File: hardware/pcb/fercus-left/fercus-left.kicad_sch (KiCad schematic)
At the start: 275 parts, among them J1 USB_C_Receptacle_USB2.0, J2 USB_C_Receptacle_USB2.0, J3 Conn_01x06_MountingPin, J5 Conn_01x03, Q1 BSS138, Q10 BSS138, Q2 BSS138, Q3 BSS138, Q4 BSS138, Q5 BSS138, Q6 BSS138, Q7 BSS138, Q8 BSS138, Q9 BSS138, SW1 SW_Push, SW2 SW_Push, SW3 SW_Push, SW4 SW_Push, SW6 SW_Push, SW7 SW_SPDT, SW8 SW_Push, U1 XC6206P332MR, U2 CH32V208CBU6, U3 ETA9084E10, Y1 32MHz, Y2 32.768kHz

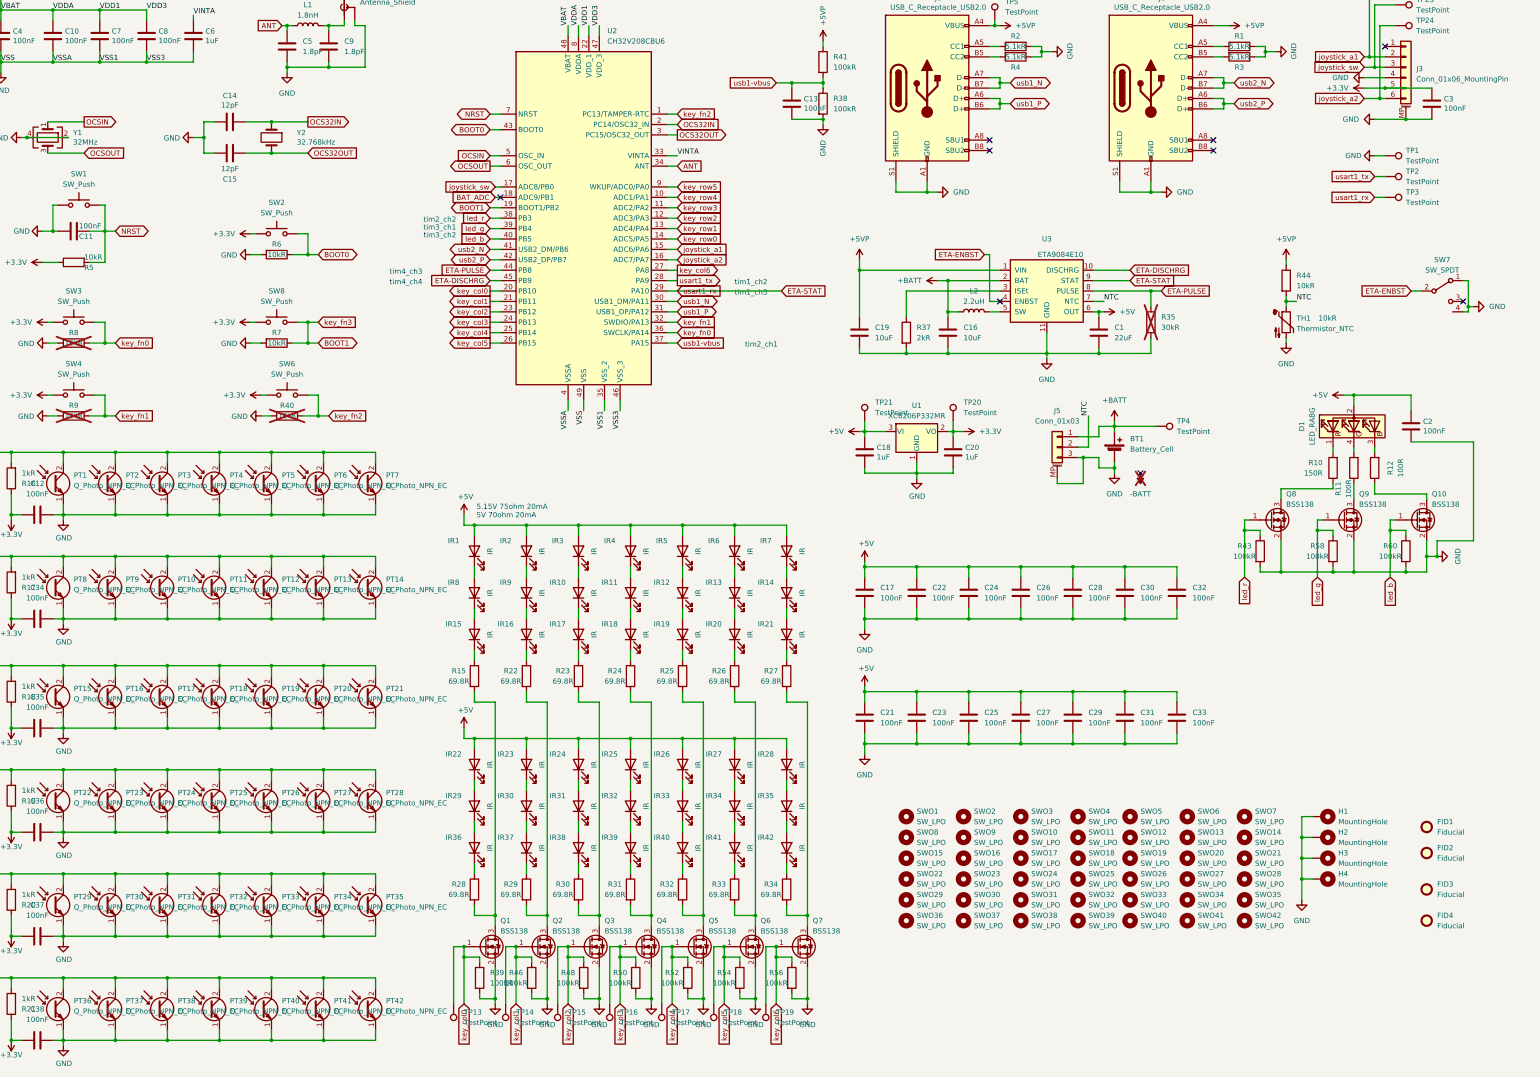
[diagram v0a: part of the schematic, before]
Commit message: merge
    fw:
    - fix usb product string, vid
    - add rf_phy_hop
    - add RF_BondingErase()
    - change default layout key fn to pause
    - fix power manager poweroff when usb disconnect
    - add usb compatibility interface

    hw:
    - change eta9084 iset resistor footprint to 0402
    - change fpc connector part
    - fix ir resistor value
    - change pcb thinkness to 1.6mm
    - fix footprint of pt and ir
    - fix rf ant trace
    - fix usb trace
    - add fercus-dongle-usb-c

    doc:
    - fix layout
    - add manual
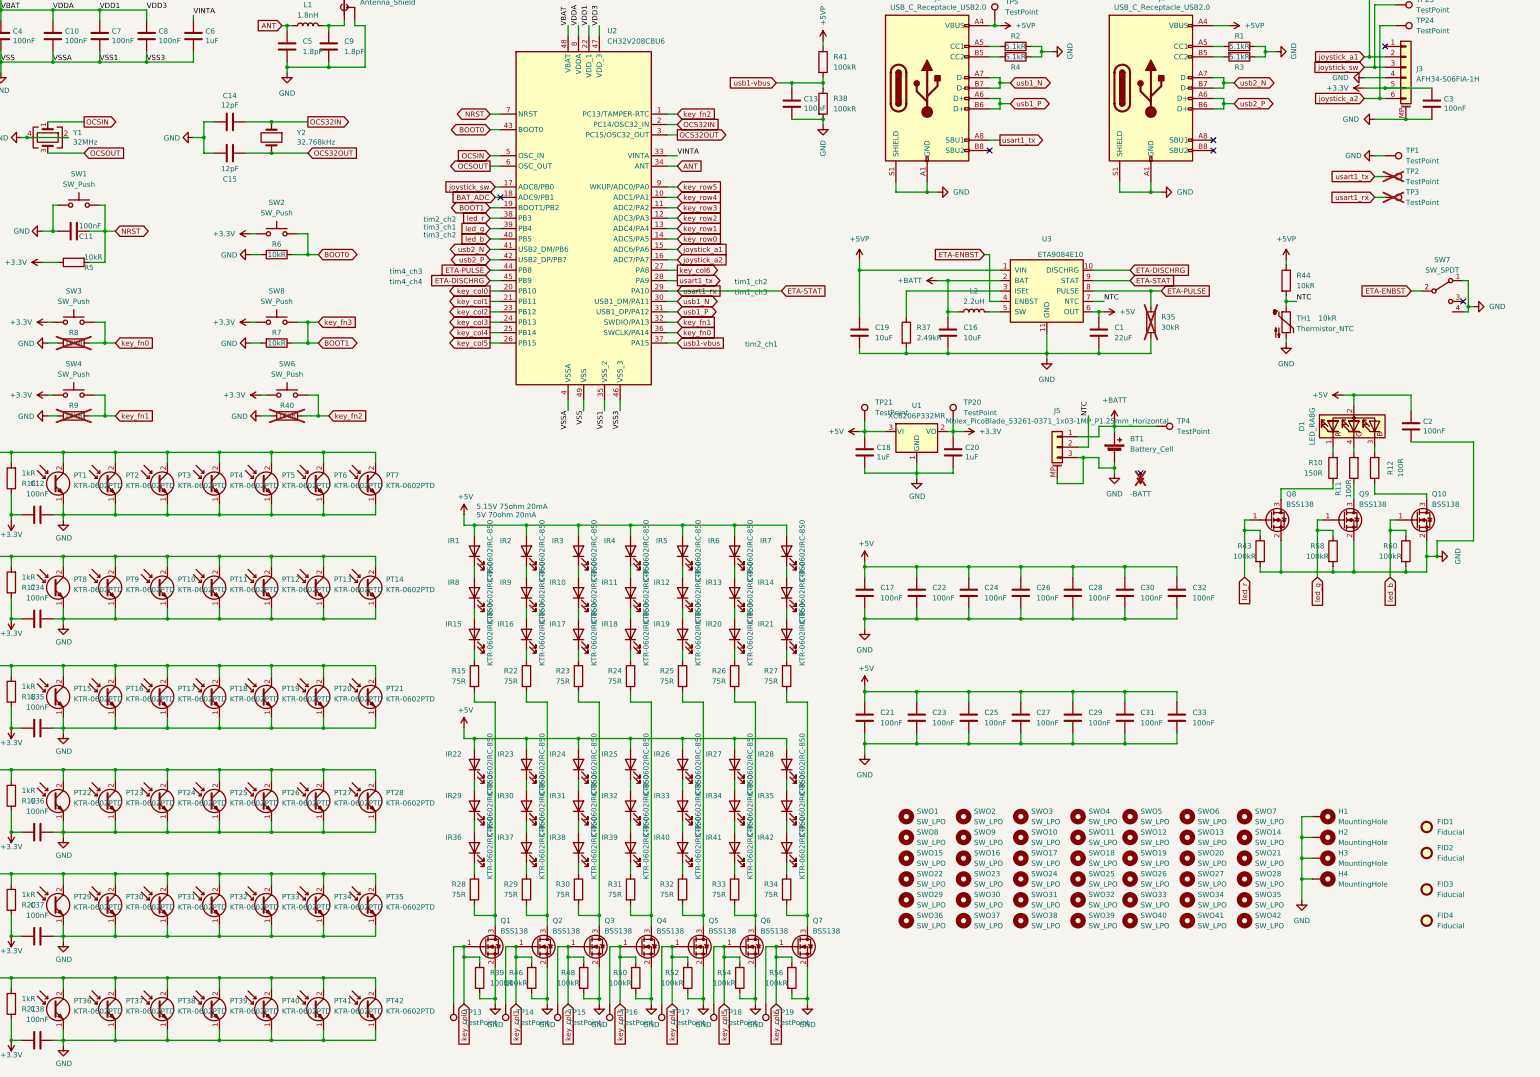
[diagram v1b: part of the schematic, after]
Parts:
- AE1: footprint chulaine:ANT-F-1-2.4G-1.2MM-FR4-WCH_Left_NoMask -> wch-ant:WCH_MIFA-1_2.4G_1.6mm_FR4_Left_NoMask
- IR1, IR10, IR11, IR12, IR13, IR14, IR15, IR16, IR17, IR18, IR19, IR2, IR20, IR21, IR22, IR23, IR24, IR25, IR26, IR27, IR28, IR29, IR3, IR30, IR31, IR32, IR33, IR34, IR35, IR36, IR37, IR38, IR39, IR4, IR40, IR41, IR42, IR5, IR6, IR7, IR8, IR9: value IR -> KTR-0602IRC-850
- J3: value Conn_01x06_MountingPin -> AFH34-S06FIA-1H
- J5: value Conn_01x03 -> Molex_PicoBlade_53261-0371_1x03-1MP_P1.25mm_Horizontal
- PT1, PT10, PT11, PT12, PT13, PT14, PT15, PT16, PT17, PT18, PT19, PT2, PT20, PT21, PT22, PT23, PT24, PT25, PT26, PT27, PT28, PT29, PT3, PT30, PT31, PT32, PT33, PT34, PT35, PT36, PT37, PT38, PT39, PT4, PT40, PT41, PT42, PT5, PT6, PT7, PT8, PT9: value Q_Photo_NPN_EC -> KTR-0602PTD
- R15, R22, R23, R24, R25, R26, R27, R28, R29, R30, R31, R32, R33, R34: value 69.8R -> 75R
- R37: value 2kR -> 2.49kR; footprint Resistor_SMD:R_0603_1608Metric -> Resistor_SMD:R_0402_1005Metric
- TP2, TP3: now not fitted
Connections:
- net usart1_tx: now also J1.A8 (SBU1)
- no-connect marks 9 -> 7

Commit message: merge
hw:
- fix sch
- fix plate
- rename to fercus-dongle-usb-a

doc:
- add assembly
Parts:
- SW1: renamed from SWO1; value SW_LPO -> SW_Optical
- SW10: renamed from SWO10; value SW_LPO -> SW_Optical
- SW11: renamed from SWO11; value SW_LPO -> SW_Optical
- SW12: renamed from SWO12; value SW_LPO -> SW_Optical
- SW13: renamed from SWO13; value SW_LPO -> SW_Optical
- SW14: renamed from SWO14; value SW_LPO -> SW_Optical
- SW15: renamed from SWO15; value SW_LPO -> SW_Optical
- SW16: renamed from SWO16; value SW_LPO -> SW_Optical
- SW17: renamed from SWO17; value SW_LPO -> SW_Optical
- SW18: renamed from SWO18; value SW_LPO -> SW_Optical
- SW19: renamed from SWO19; value SW_LPO -> SW_Optical
- SW2: renamed from SWO2; value SW_LPO -> SW_Optical
- SW20: renamed from SWO20; value SW_LPO -> SW_Optical
- SW21: renamed from SWO21; value SW_LPO -> SW_Optical
- SW22: renamed from SWO22; value SW_LPO -> SW_Optical
- SW23: renamed from SWO23; value SW_LPO -> SW_Optical
- SW24: renamed from SWO24; value SW_LPO -> SW_Optical
- SW25: renamed from SWO25; value SW_LPO -> SW_Optical
- SW26: renamed from SWO26; value SW_LPO -> SW_Optical
- SW27: renamed from SWO27; value SW_LPO -> SW_Optical
- SW28: renamed from SWO28; value SW_LPO -> SW_Optical
- SW29: renamed from SWO29; value SW_LPO -> SW_Optical
- SW3: renamed from SWO3; value SW_LPO -> SW_Optical
- SW30: renamed from SWO30; value SW_LPO -> SW_Optical
- SW31: renamed from SWO31; value SW_LPO -> SW_Optical
- SW32: renamed from SWO32; value SW_LPO -> SW_Optical
- SW33: renamed from SWO33; value SW_LPO -> SW_Optical
- SW34: renamed from SWO34; value SW_LPO -> SW_Optical
- SW35: renamed from SWO35; value SW_LPO -> SW_Optical
- SW36: renamed from SWO36; value SW_LPO -> SW_Optical
- SW37: renamed from SWO37; value SW_LPO -> SW_Optical
- SW38: renamed from SWO38; value SW_LPO -> SW_Optical
- SW39: renamed from SWO39; value SW_LPO -> SW_Optical
- SW4: renamed from SWO4; value SW_LPO -> SW_Optical
- SW40: renamed from SWO40; value SW_LPO -> SW_Optical
- SW41: renamed from SWO41; value SW_LPO -> SW_Optical
- SW42: renamed from SWO42; value SW_LPO -> SW_Optical
- SW49: renamed from SW7; footprint chulaine:SW_SPDT_PCM12_Vertical -> chulaine:SW_SPDT_PCM12
- SW5: renamed from SWO5; value SW_LPO -> SW_Optical
- SW6: renamed from SWO6; value SW_LPO -> SW_Optical
- SW7: renamed from SWO7; value SW_LPO -> SW_Optical
- SW8: renamed from SWO8; value SW_LPO -> SW_Optical
- SW9: renamed from SWO9; value SW_LPO -> SW_Optical
- renumbered C12 to C21, C34 to C22, C35 to C23, C36 to C24, C37 to C25, C38 to C26, C21 to C31, C23 to C32, C25 to C33, C27 to C34, C29 to C35, C31 to C36, C33 to C37, C17 to C38, C22 to C39, C24 to C40, C26 to C41, C28 to C42, C30 to C43, C32 to C44, IR1 to D1, IR10 to D10, IR11 to D11, IR12 to D12, IR13 to D13, IR14 to D14, IR15 to D15, IR16 to D16, IR17 to D17, IR18 to D18, IR19 to D19, IR2 to D2, IR20 to D20, IR21 to D21, IR22 to D22, IR23 to D23, IR24 to D24, IR25 to D25, IR26 to D26, IR27 to D27, IR28 to D28, IR29 to D29, IR3 to D3, IR30 to D30, IR31 to D31, IR32 to D32, IR33 to D33, IR34 to D34, IR35 to D35, IR36 to D36, IR37 to D37, IR38 to D38, IR39 to D39, IR4 to D4, IR40 to D40, IR41 to D41, IR42 to D42, D1 to D43, IR5 to D5, IR6 to D6, IR7 to D7, IR8 to D8, IR9 to D9, PT1 to Q1, PT10 to Q10, PT11 to Q11, PT12 to Q12, PT13 to Q13, PT14 to Q14, PT15 to Q15, PT16 to Q16, PT17 to Q17, PT18 to Q18, PT19 to Q19, PT2 to Q2, PT20 to Q20, PT21 to Q21, PT22 to Q22, PT23 to Q23, PT24 to Q24, PT25 to Q25, PT26 to Q26, PT27 to Q27, PT28 to Q28, PT29 to Q29, PT3 to Q3, PT30 to Q30, PT31 to Q31, PT32 to Q32, PT33 to Q33, PT34 to Q34, PT35 to Q35, PT36 to Q36, PT37 to Q37, PT38 to Q38, PT39 to Q39, PT4 to Q4, PT40 to Q40, PT41 to Q41, PT42 to Q42, Q1 to Q43, Q2 to Q44, Q3 to Q45, Q4 to Q46, Q5 to Q47, Q6 to Q48, Q7 to Q49, PT5 to Q5, Q8 to Q50, Q9 to Q51, Q10 to Q52, PT6 to Q6, PT7 to Q7, PT8 to Q8, PT9 to Q9, SW1 to SW43, SW2 to SW44, SW8 to SW45, SW3 to SW46, SW4 to SW47, SW6 to SW48
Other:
- moved on the sheet: AE1, BT1, C11, C13, C14, C15, C18, C2, C20, C21, C22, C23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
